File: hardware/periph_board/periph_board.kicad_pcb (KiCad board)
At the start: 2 copper layers, 149.7 x 25 mm, 49 parts, among them IC100 CD74HC4067SM96, IC101 LM2937ET-3.3_NOPB, IC102 ADC121S021CIMFX_NOPB, J100 2x10 Male Pins, U200 AH49HNTR-G1, U201 AH49HNTR-G1, U202 AH49HNTR-G1, U203 AH49HNTR-G1, U204 AH49HNTR-G1, U205 AH49HNTR-G1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

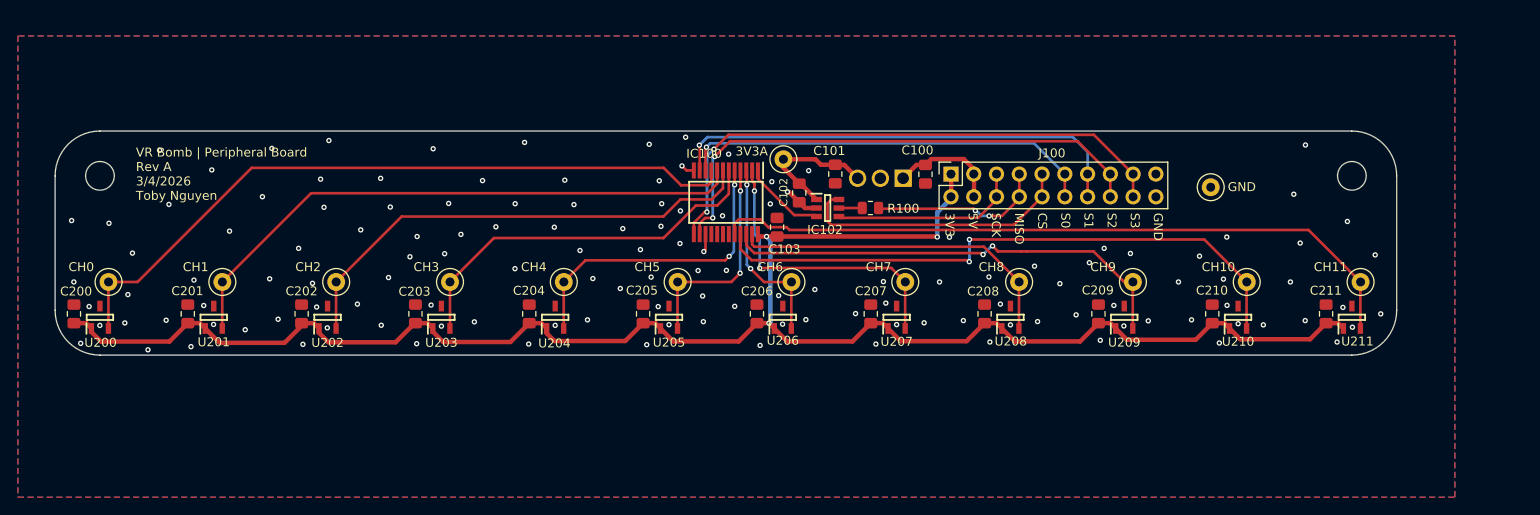
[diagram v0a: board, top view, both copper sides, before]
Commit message: Adjusted spacing to 13.5mm between hall effects
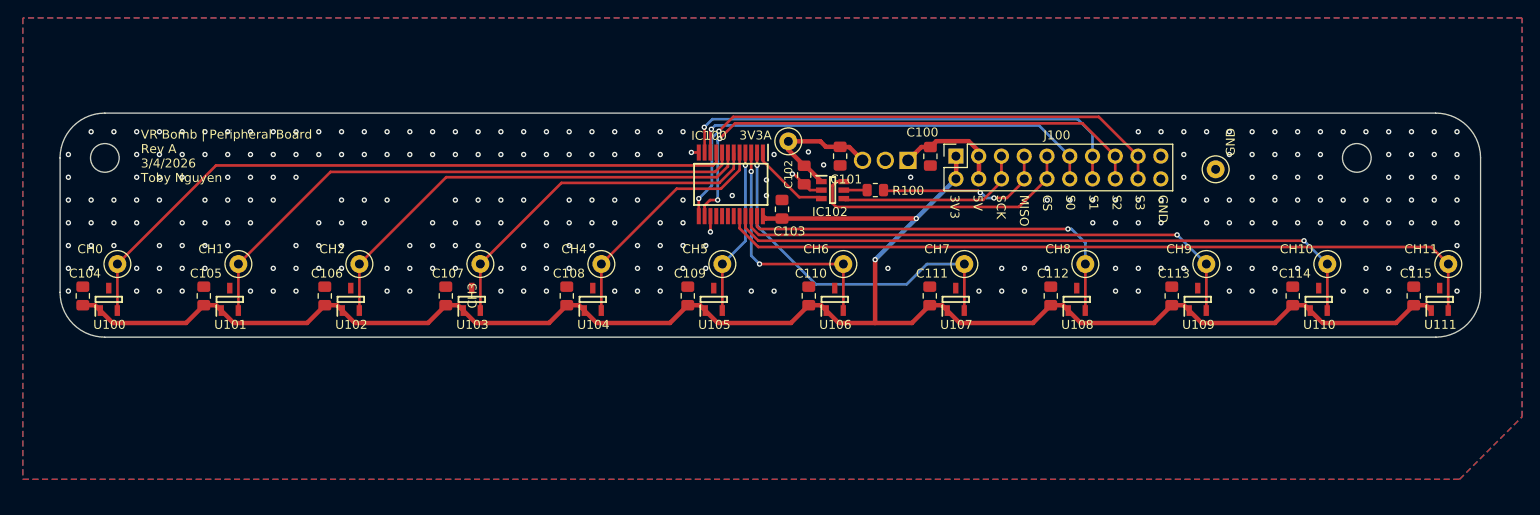
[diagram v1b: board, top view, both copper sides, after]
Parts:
- removed C201, C202, C203, C204, C205, C206, C207, C208, C209, C210, C211: 1u, Capacitor_SMD:C_0805_2012Metric_Pad1.18x1.45mm_HandSolder
- removed TP114: CH10, SamacSys_Parts:bettertestpoint2
- removed TP115: CH11, SamacSys_Parts:bettertestpoint2
- removed U201, U202, U203, U204, U205, U206, U207, U208, U209, U210, U211: AH49HNTR-G1, SamacSys_Parts:SOT95P282X145-3N
- added C105: 1u, Capacitor_SMD:C_0805_2012Metric_Pad1.18x1.45mm_HandSolder, F.Cu at (93.0, 93.0)
- added C106: 1u, Capacitor_SMD:C_0805_2012Metric_Pad1.18x1.45mm_HandSolder, F.Cu at (106.5, 93.0)
- added C107: 1u, Capacitor_SMD:C_0805_2012Metric_Pad1.18x1.45mm_HandSolder, F.Cu at (120.0, 93.0)
- added C108: 1u, Capacitor_SMD:C_0805_2012Metric_Pad1.18x1.45mm_HandSolder, F.Cu at (133.5, 93.0)
- added C109: 1u, Capacitor_SMD:C_0805_2012Metric_Pad1.18x1.45mm_HandSolder, F.Cu at (147.0, 93.0)
- added C110: 1u, Capacitor_SMD:C_0805_2012Metric_Pad1.18x1.45mm_HandSolder, F.Cu at (160.5, 93.0)
- added C111: 1u, Capacitor_SMD:C_0805_2012Metric_Pad1.18x1.45mm_HandSolder, F.Cu at (174.0, 93.0)
- added C112: 1u, Capacitor_SMD:C_0805_2012Metric_Pad1.18x1.45mm_HandSolder, F.Cu at (187.5, 93.0)
- added C113: 1u, Capacitor_SMD:C_0805_2012Metric_Pad1.18x1.45mm_HandSolder, F.Cu at (201.0, 93.0)
- added C114: 1u, Capacitor_SMD:C_0805_2012Metric_Pad1.18x1.45mm_HandSolder, F.Cu at (214.5, 93.0)
- added C115: 1u, Capacitor_SMD:C_0805_2012Metric_Pad1.18x1.45mm_HandSolder, F.Cu at (228.0, 93.0)
- added TP101: CH1, SamacSys_Parts:bettertestpoint2, F.Cu at (96.8, 89.4)
- added TP104: CH4, SamacSys_Parts:bettertestpoint2, F.Cu at (137.3, 89.4)
- added U101: AH49HNTR-G1, SamacSys_Parts:SOT95P282X145-3N, F.Cu at (95.9, 93.4)
- added U102: AH49HNTR-G1, SamacSys_Parts:SOT95P282X145-3N, F.Cu at (109.4, 93.4)
- added U103: AH49HNTR-G1, SamacSys_Parts:SOT95P282X145-3N, F.Cu at (122.9, 93.4)
- added U104: AH49HNTR-G1, SamacSys_Parts:SOT95P282X145-3N, F.Cu at (136.4, 93.4)
- added U105: AH49HNTR-G1, SamacSys_Parts:SOT95P282X145-3N, F.Cu at (149.9, 93.4)
- added U106: AH49HNTR-G1, SamacSys_Parts:SOT95P282X145-3N, F.Cu at (163.4, 93.4)
- added U107: AH49HNTR-G1, SamacSys_Parts:SOT95P282X145-3N, F.Cu at (176.9, 93.4)
- added U108: AH49HNTR-G1, SamacSys_Parts:SOT95P282X145-3N, F.Cu at (190.4, 93.4)
- added U109: AH49HNTR-G1, SamacSys_Parts:SOT95P282X145-3N, F.Cu at (203.9, 93.4)
- added U110: AH49HNTR-G1, SamacSys_Parts:SOT95P282X145-3N, F.Cu at (217.4, 93.4)
- added U111: AH49HNTR-G1, SamacSys_Parts:SOT95P282X145-3N, F.Cu at (230.9, 93.4)
- C101: value 1u -> 10u
- TP102: value CH1 -> CH2
- TP103: value 3V3A -> CH3
- TP105: value CH2 -> CH5
- TP106: value CH3 -> CH6
- TP107: value CH4 -> CH7
- TP108: value CH5 -> CH8
- TP109: value CH6 -> CH9
- TP110: value GND -> CH10
- TP111: value CH7 -> CH11
- TP112: value CH8 -> GND
- TP113: value CH9 -> 3V3A
- moved TP111 60.6 mm to (231.8, 89.4)
- moved TP109 46.3 mm to (204.8, 89.4)
- moved TP108 45.5 mm to (191.3, 89.4)
- moved TP107 44.7 mm to (177.8, 89.4)
- moved TP106 43.9 mm to (164.3, 89.4)
- moved TP105 43.1 mm to (150.8, 89.4)
- moved TP113 41.5 mm to (158.2, 75.8), turned to 0 degrees
- moved TP103 35.8 mm to (123.8, 89.4), turned to 90 degrees
- moved TP112 25.3 mm to (205.9, 78.9), turned to 0 degrees
- moved TP110 15.6 mm to (218.3, 89.4), turned to 90 degrees
- moved TP102 15.4 mm to (110.3, 89.4)
- moved C104 2.23 mm to (79.5, 93.0)
- moved TP100 2.23 mm to (83.3, 89.4)
- moved U100 2.23 mm to (82.4, 93.4)
- moved C102 2.07 mm to (160.0, 79.5)
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- renumbered C200 to C104, U200 to U100
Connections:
- C101 pad 1: GND -> +3.3VADC
- C101 pad 2: +3.3VADC -> GND
- TP102 pad 1: /CH1 -> /CH2
- TP103 pad 1: +3.3VADC -> /CH3
- TP105 pad 1: /CH2 -> /CH5
- TP106 pad 1: /CH3 -> /CH6
- TP107 pad 1: /CH4 -> /CH7
- TP108 pad 1: /CH5 -> /CH8
- TP109 pad 1: /CH6 -> /CH9
- TP110 pad 1: GND -> /CH10
- TP111 pad 1: /CH7 -> /CH11
- TP112 pad 1: /CH8 -> GND
- TP113 pad 1: /CH9 -> +3.3VADC
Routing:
- net +3V3: track 198.8 -> 208.3 mm, vias 3 -> 2
- net /CH8: track 37.9 -> 46.1 mm, vias 0 -> 1
- net /CH11: track 79.3 -> 87.3 mm
- net /CH4: track 34.7 -> 26.9 mm, vias 2 -> 0
- net /CH9: track 52.1 -> 58.9 mm, vias 2 -> 1
- net /CH7: track 33.4 -> 40.1 mm, vias 2 -> 1
- net /CH6: track 21.5 -> 27.4 mm
- net /CH5: track 24.1 -> 18.7 mm, vias 2 -> 1
- net /CH10: track 68.4 -> 73.1 mm, vias 2 -> 1
- net /CH3: track 43.0 -> 39.6 mm
- net /CH2: track 54.7 -> 52.3 mm
- net /CH0: track 80.0 -> 77.8 mm
- net /CH1: track 66.4 -> 65.1 mm
- net GND: track 7.56 -> 6.58 mm, vias 137 -> 270
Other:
- board size 149.7 x 25 mm -> 158.5 x 25 mm
